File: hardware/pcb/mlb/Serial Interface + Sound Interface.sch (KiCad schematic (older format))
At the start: 52 parts, among them J1 Phone Jack, J11 Speaker, J2 SERIAL_CONN, J3 SERIAL_CONN, Q1 2N3904, Q2 2N3906, Y3 16.9344MHz

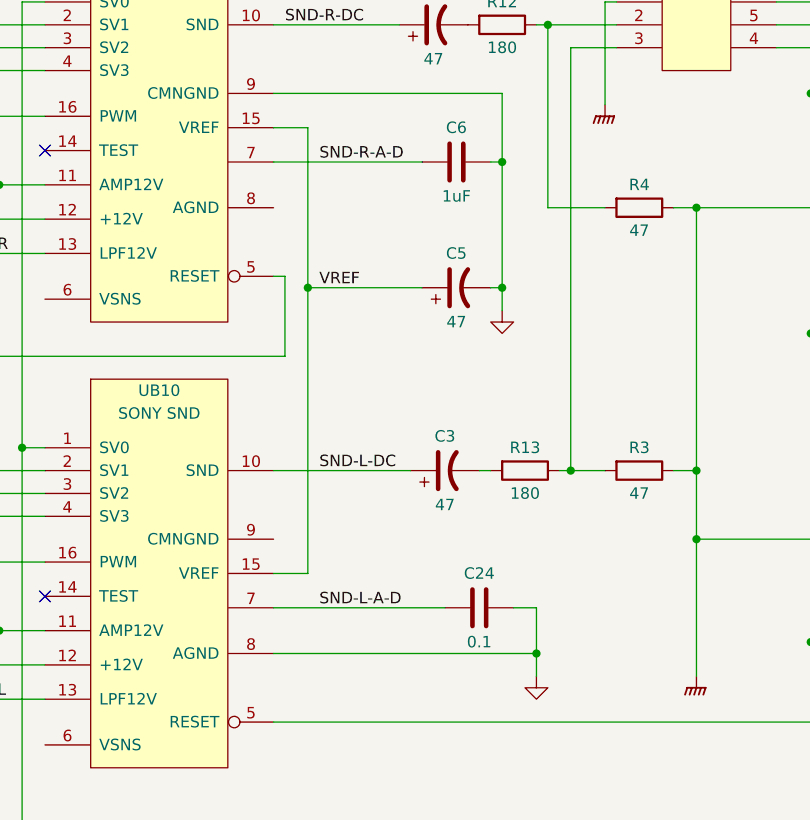
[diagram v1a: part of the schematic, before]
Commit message: Fix missing ground wires, fix some missing reference designators.
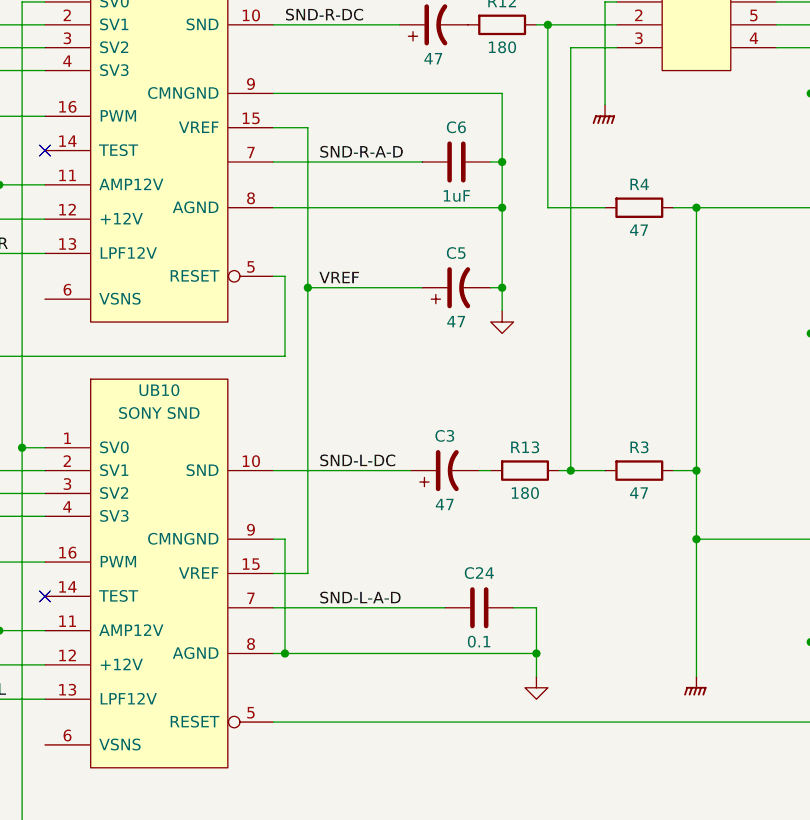
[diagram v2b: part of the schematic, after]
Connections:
- net GND: now also UB10.9 (CMNGND), UB11.8 (AGND)
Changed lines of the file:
@@
 Connection ~ 11850 6750
 Wire Wire Line
-	11850 6750 11850 7300
+	11850 6750 11850 6950
 Wire Wire Line
 	11800 7300 11850 7300
@@
 $EndComp
 Wire Wire Line
-	10850 8900 12000 8900
+	10850 8900 10900 8900
 Wire Wire Line
 	11900 8700 12000 8700
@@
 Wire Bus Line
 	2200 3200 1350 3200
-Wire Bus Line
-	2050 2900 2050 9200
-Wire Bus Line
-	2200 3200 2200 7900
 Text Notes 16195 735  0    50   ~ 0
 (8)
@@
 Text Notes 1010 735  2    50   ~ 0
 (8)
+Wire Wire Line
+	10850 6950 11850 6950
+Connection ~ 11850 6950
+Wire Wire Line
+	11850 6950 11850 7300
+Wire Wire Line
+	10850 8400 10900 8400
+Wire Wire Line
+	10900 8400 10900 8900
+Wire Bus Line
+	2050 2900 2050 9200
+Wire Bus Line
+	2200 3200 2200 7900
+Connection ~ 10900 8900
+Wire Wire Line
+	10900 8900 12000 8900
 $EndSCHEMATC

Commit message: Correct transcription error DSC to OSC.
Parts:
- UE10: value DSC -> OSC; symbol Macintosh_SE_30_Components:DSC -> Macintosh_SE_30_Components:OSC
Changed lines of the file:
@@
 NoConn ~ 3750 7800
 $Comp
-L Macintosh_SE_30_Components:DSC UE10
+L Macintosh_SE_30_Components:OSC UE10
 U 1 1 5EC30FDA
 P 3200 6950
 F 0 "UE10" H 3200 6850 50  0000 C CNN
-F 1 "DSC" H 3200 6750 50  0000 C CNN
+F 1 "OSC" H 3200 6750 50  0000 C CNN
 F 2 "" H 3200 6950 50  0001 C CNN
 F 3 "" H 3200 6950 50  0001 C CNN

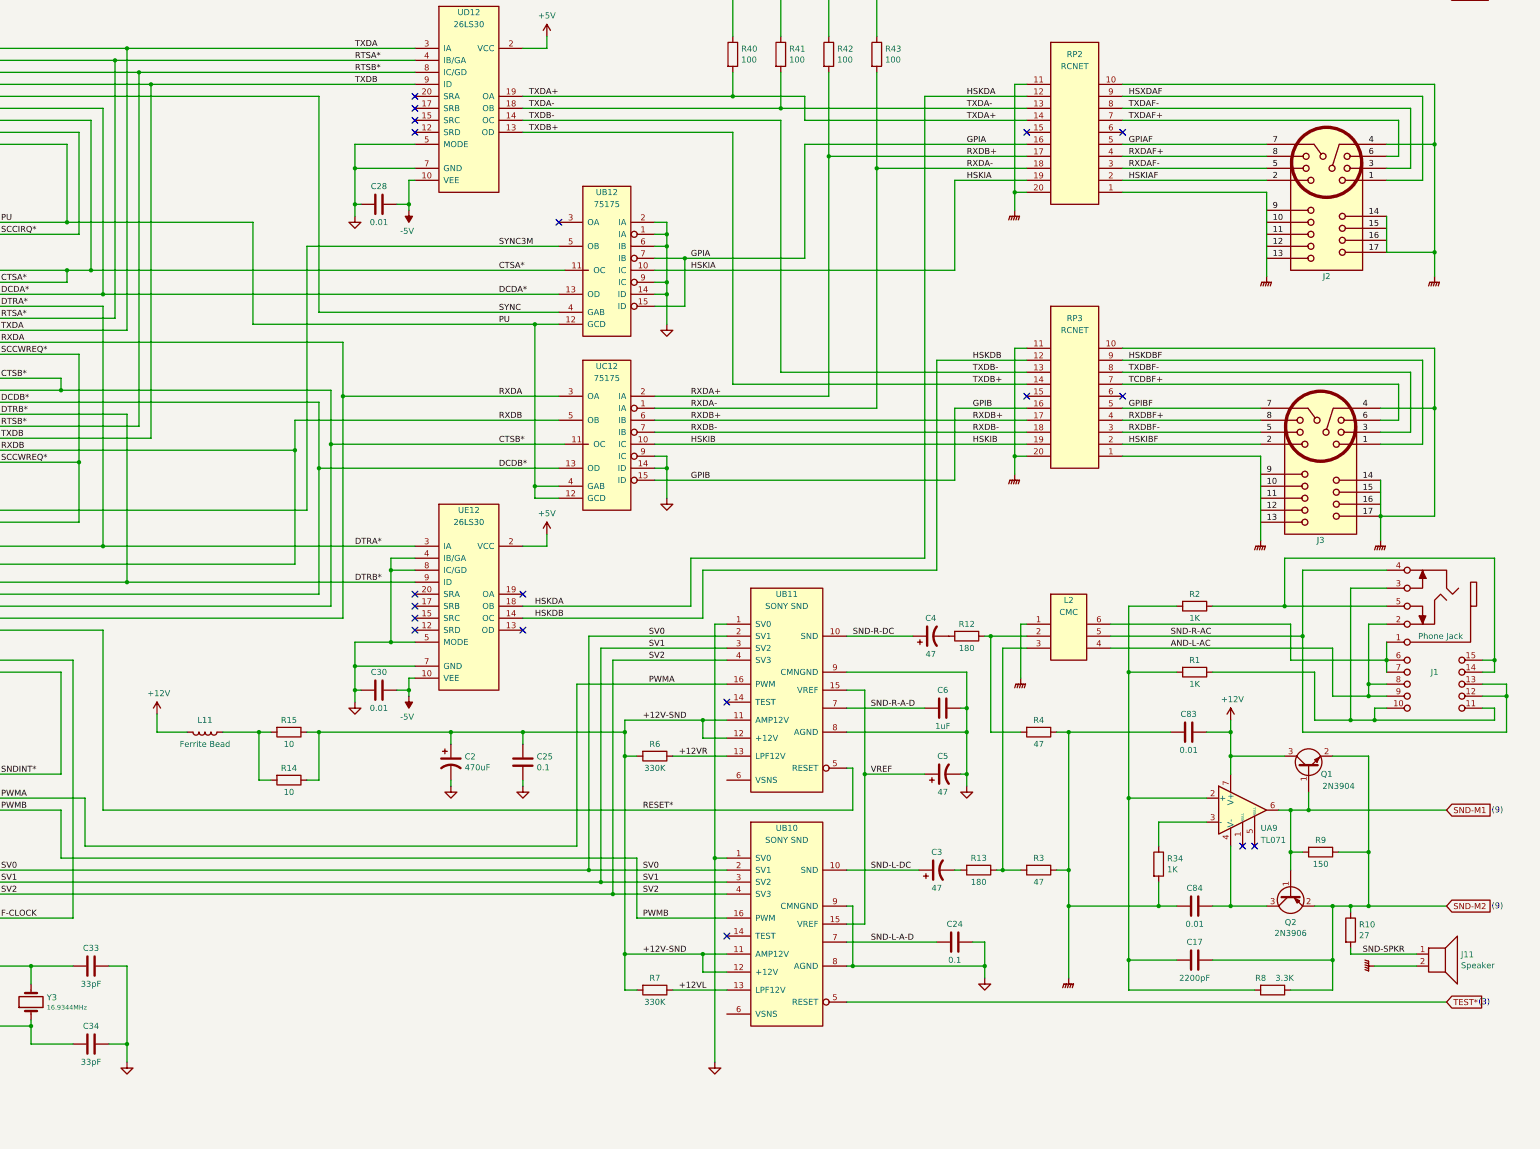
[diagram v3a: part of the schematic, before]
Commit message: Fix errors found in review of the Macintosh SE/30 schematic redraw.
Page 1:

* DSACK*(0:1) (syntax)
* R-W* (inconsistent syntax)
* IPL different syntax
* PDS 38, C16M not grounded
* PDS 39, should be grounded

Page 2:

* RAAF*(8), RABF*(9), RAAF*(10), RABF*(10) (syntax)
* RCMUX* (syntax)
* ROM* missing page 3 indicator
* ROMSIMM1 GND 10, 30, 64
* ROMSIMM1 Incorrect +5V lines
* ROMSIMM1 Confusing bus line drawing angles makes connections look
  duplicated

Page 3:

* VIAIRQ2* (syntax)
* VIAIRQ1N (syntax, on GLUE template)
* SCCRD* (syntax)

Page 4:

* VIA template, RS0, RS1, RS2, RS3 erroneously written as R50, R51,
  R52, R53
* V1PB7 erroneously written as VIPB7
* RTC-D erroneously written as RTC-O
* V1PA0, V1PA1, V1PA2 erroneously written as VIPA0, VIPA1, VIPA2
* warning: additional label BATT not present
* UL11 ADB template, P5 erroneously written as P2
* ADBO erroneously written as ADB0
* SNDINT* erroneously written as SNTINT*

Page 5:

* HSYNC* on UG7 (syntax)
* UJ6 confusing bus line makes signals look duplicated
* Video ROM UK6 not labeled with reference designator (already inside
  KiCad file, stale PDF?)
* VIDS4, VIDS3, VIDS2, VIDS1, VIDS0 erroneously written a VID54,
  VID53, VID53, VID51, VID50
* R-W* alternate page reference erroneously written as RW*
* 74F253 template, G erroneously labeled as GND
* 74F253 template, missing second G enable pin
* style: C0 in 74F253 template should not be C0(GND)
* warning: UA8 ALTVID line could have another label close to the chip

Page 6:

* warning: On SWIM, WRDATA could have label WR*
* DB25 connector: DP*, DB0*, DB1*, DB2*, DB3*, DB4*, DB5*, DB6*, DB7*
  (syntax)
* J8 Ribbon Connector: Missing +12V on 13, 15, 17, 19
* J6 DB-19: Missing +12V-DSK on 7, 8
* warning: missing RDDATA.F additional label near J6 DB-19 pin 18
* warning: missing WRITE.F additional label near J6 DB-19 pin 19
* warning: confusing bus line layout on 53C80 looks like duplicate
  wiring

Page 7:

* RXDA+ erroneously written as RXDB+
* HSKOA erroneo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
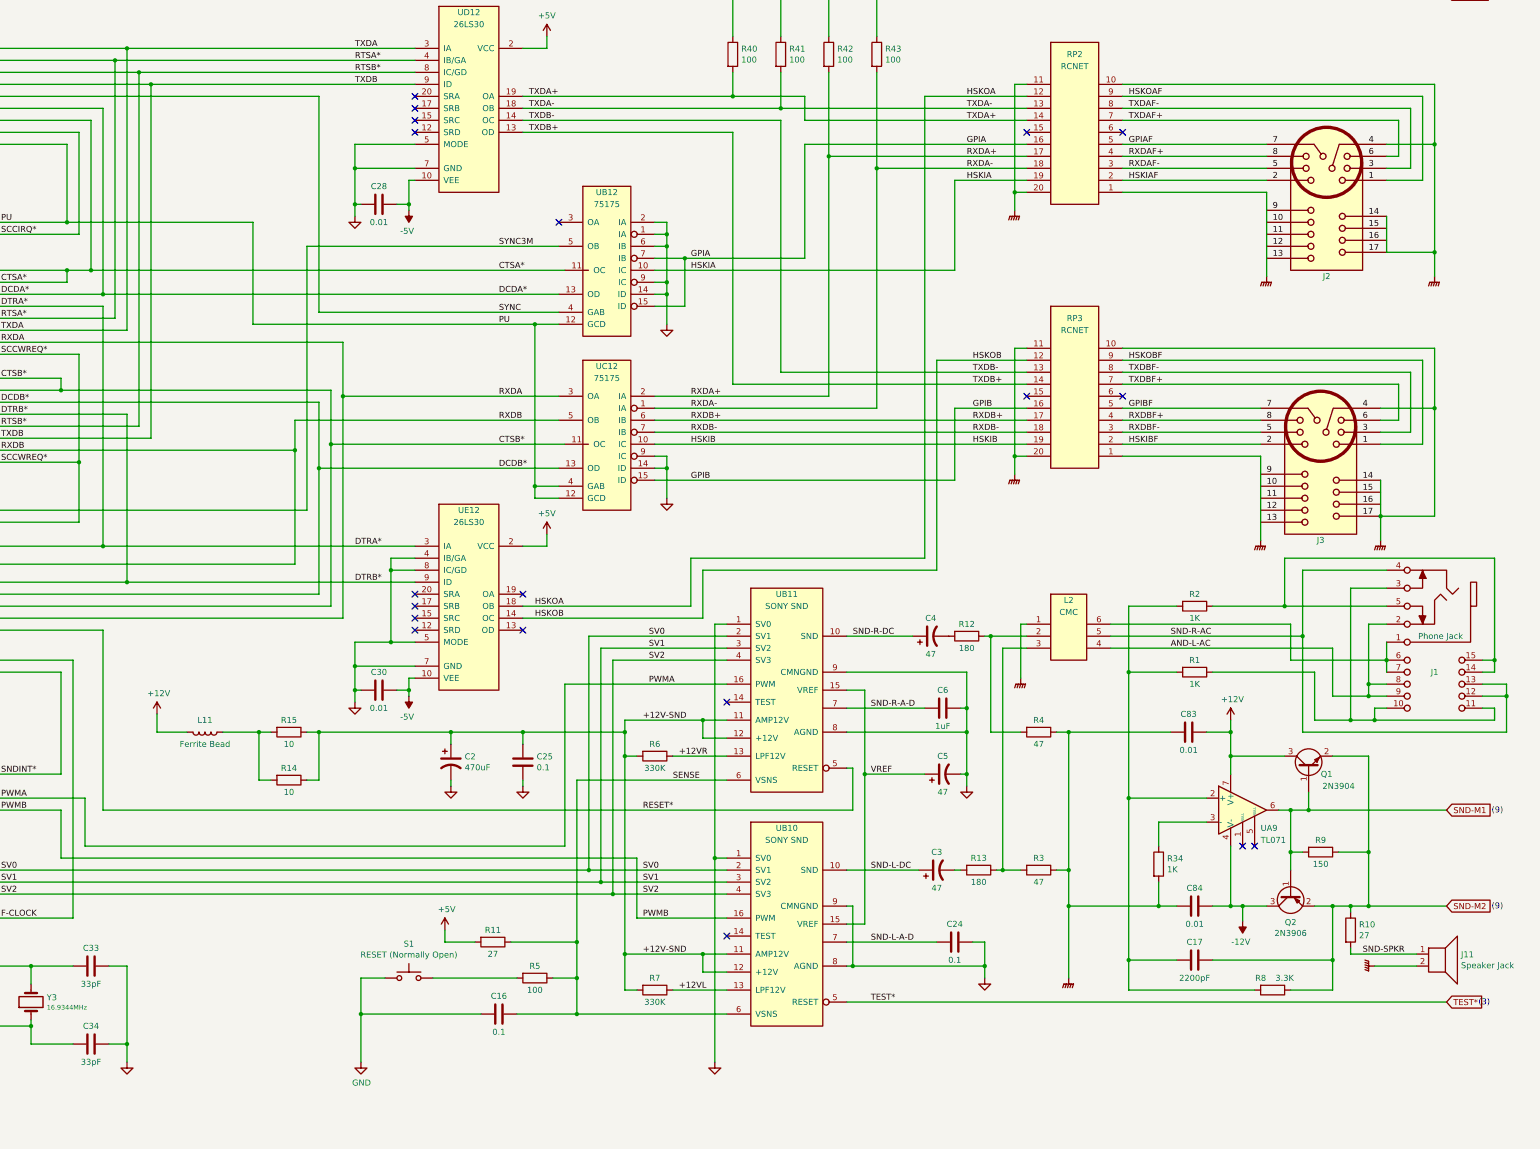
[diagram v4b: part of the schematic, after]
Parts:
- added C16: 0.1, symbol Device:C
- added R11: 27, symbol Device:R
- added R5: 100, symbol Device:R
- added S1: RESET (Normally Open), symbol Switch:SW_MEC_5G
- J11: value Speaker -> Speaker Jack
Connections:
- net +5V: now also R11.2
- net GND: now also C16.2, S1.1 (A), S1.2 (A)
- net RXDA+: no longer RP3.17, UC12.6 (IB)
- net SENSE: now reaches UB11.6 (VSNS)
- net SENSE: now also UB10.6 (VSNS), C16.1, R11.1, R5.1
- net -12V: now reaches C84.1, Q2.3 (E), UA9.4 (V-)
- net HSKDA renamed HSKOA
- net HSKDB renamed HSKOB
- net HSKDBF renamed HSKOBF
- net HSXDAF renamed HSKOAF
- net TCDBF+ renamed TXDBF+
- new net: R5.2, S1.3 (B), S1.4 (B)
- new net RXDB+: RP3.17, UC12.6 (IB)
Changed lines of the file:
@@
 U 1 1 5EC30DA6
 P 3200 2450
+AR Path="/5EC30DA6" Ref="UG12"  Part="1"
+AR Path="/5EC6E3D0/5EC30DA6" Ref="UG12"  Part="1"
 F 0 "UG12" H 3200 2550 50  0000 C CNN
 F 1 "8530" H 3200 2450 50  0000 C CNN
@@
 U 1 1 5EC34042
 P 8850 2550
+AR Path="/5EC34042" Ref="UB12"  Part="1"
+AR Path="/5EC6E3D0/5EC34042" Ref="UB12"  Part="1"
 F 0 "UB12" H 8850 2650 50  0000 C CNN
 F 1 "75175" H 8850 2550 50  0000 C CNN
@@
 U 1 1 5EC340B3
 P 8850 4000
+AR Path="/5EC340B3" Ref="UC12"  Part="1"
+AR Path="/5EC6E3D0/5EC340B3" Ref="UC12"  Part="1"
 F 0 "UC12" H 8850 4100 50  0000 C CNN
 F 1 "75175" H 8850 4000 50  0000 C CNN
@@
 	4500 7500 4500 7900
 Wire Wire Line
-	4500 7900 8600 7900
+	4500 7900 8500 7900
 Wire Wire Line
-	8600 7900 8600 6550
+	8500 7900 8500 6550
 Wire Wire Line
-	8600 6550 9850 6550
+	8500 6550 9850 6550
 Text Label 9200 6550 0    50   ~ 0
 PWMA
@@
 Connection ~ 14050 8400
 Wire Wire Line
-	14050 8400 14350 8400
+	14050 8400 14150 8400
 $Comp
 L Macintosh_SE_30_Components:2N3906 Q2
@@
 	0    1    1    0
 $EndComp
-$Comp
-L Device:Speaker J11
-U 1 1 5F089CF2
-P 15800 8800
-F 0 "J11" H 15970 8796 50  0000 L CNN
-F 1 "Speaker" H 15970 8705 50  0000 L CNN
-F 2 "" H 15800 8600 50  0001 C CNN
-F 3 "~" H 15790 8750 50  0001 C CNN
-	1    15800 8800
-	1    0    0    -1
-$EndComp
 Text Label 15150 8800 0    50   ~ 0
 SND-SPKR
@@
 RXDA-
 Text Label 11850 2150 0    50   ~ 0
-RXDB+
+RXDA+
 Text Label 11850 2050 0    50   ~ 0
 GPIA
@@
 TXDA-
 Text Label 11850 1650 0    50   ~ 0
-HSKDA
+HSKOA
 Text Label 9550 3000 0    50   ~ 0
 GPIA
@@
 	9650 5600 11600 5600
 Text Label 11900 3850 0    50   ~ 0
-HSKDB
+HSKOB
 Text Label 8250 5900 0    50   ~ 0
-HSKDA
+HSKOA
 Text Label 8250 6000 0    50   ~ 0
-HSKDB
+HSKOB
 Wire Wire Line
 	9900 800  1350 800
@@
 $EndComp
 Text Label 13200 1650 0    50   ~ 0
-HSXDAF
+HSKOAF
 Text Label 13200 1750 0    50   ~ 0
 TXDAF-
@@
 	15750 4250 15750 5150
 Text Label 13200 3850 0    50   ~ 0
-HSKDBF
+HSKOBF
 Text Label 13200 3950 0    50   ~ 0
 TXDBF-
 Text Label 13200 4050 0    50   ~ 0
-TCDBF+
+TXDBF+
 Text Label 13200 4250 0    50   ~ 0
 GPIBF
@@
 Wire Wire Line
 	10900 8400 10900 8900
+Connection ~ 10900 8900
+Wire Wire Line
+	10900 8900 12000 8900
+$Comp
+L power:-12V #PWR?
+U 1 1 606E34BB
+P 14150 8525
+F 0 "#PWR?" H 14150 8625 50  0001 C CNN
+F 1 "-12V" H 14165 8698 50  0000 C CNN
+F 2 "" H 14150 8525 50  0001 C CNN
+F 3 "" H 14150 8525 50  0001 C CNN
+	1    14150 8525
+	-1   0    0    1
+$EndComp
+Connection ~ 14150 8400
+Wire Wire Line
+	14150 8400 14350 8400
+Wire Wire Line
+	14150 8525 14150 8400
+$Comp
+L Device:Speaker J11
+U 1 1 5F089CF2
+P 15800 8800
+F 0 "J11" H 15970 8796 50  0000 L CNN
+F 1 "Speaker Jack" H 15970 8705 50  0000 L CNN
+F 2 "" H 15800 8600 50  0001 C CNN
+F 3 "~" H 15790 8750 50  0001 C CNN
+	1    15800 8800
+	1    0    0    -1
+$EndComp
+$Comp
+L Device:R R11
+U 1 1 6086FEE8
+P 7900 8700
+F 0 "R11" V 7800 8700 50  0000 C CNN
+F 1 "27" V 8000 8700 50  0000 C CNN
+F 2 "" V 7830 8700 50  0001 C CNN
+F 3 "~" H 7900 8700 50  0001 C CNN
+	1    7900 8700
+	0    1    1    0
+$EndComp
+$Comp
+L Device:C C16
+U 1 1 608F0E76
+P 7950 9300
+F 0 "C16" V 7800 9300 50  0000 C CNN
+F 1 "0.1" V 8100 9300 50  0000 C CNN
+F 2 "" H 7988 9150 50  0001 C CNN
+F 3 "~" H 7950 9300 50  0001 C CNN
+	1    7950 9300
+	0    1    1    0
+$EndComp
+$Comp
+L power:GND #PWR?
+U 1 1 609342BB
+P 6800 9700
+F 0 "#PWR?" H 6800 9450 50  0001 C CNN
+F 1 "GND" H 6805 9527 50  0000 C CNN
+F 2 "" H 6800 9700 50  0001 C CNN
+F 3 "" H 6800 9700 50  0001 C CNN
+	1    6800 9700
+	1    0    0    -1
+$EndComp
+$Comp
+L Switch:SW_MEC_5G S1
+U 1 1 609B70E2
+P 7200 9000
+F 0 "S1" H 7200 9285 50  0000 C CNN
+F 1 "RESET (Normally Open)" H 7200 9194 50  0000 C CNN
+F 2 "" H 7200 9200 50  0001 C CNN
+F 3 "http://www.apem.com/int/index.php?controller=attachment&id_attachment=488" H 7200 9200 50  0001 C CNN
+	1    7200 9000
+	1    0    0    -1
+$EndComp
+$Comp
+L power:+5V #PWR?
+U 1 1 609B8E47
+P 7500 8600
+F 0 "#PWR?" H 7500 8450 50  0001 C CNN
+F 1 "+5V" H 7515 8773 50  0000 C CNN
+F 2 "" H 7500 8600 50  0001 C CNN
+F 3 "" H 7500 8600 50  0001 C CNN
+	1    7500 8600
+	1    0    0    -1
+$EndComp
+Wire Wire Line
+	7500 8600 7500 8700
+Wire Wire Line
+	7500 8700 7750 8700
+Wire Wire Line
+	8100 9000 7400 9000
+Wire Wire Line
+	7000 9000 6800 9000
+Wire Wire Line
+	6800 9000 6800 9300
+Wire Wire Line
+	7800 9300 6800 9300
+Connection ~ 6800 9300
+Wire Wire Line
+	6800 9300 6800 9700
+Wire Wire Line
+	9850 9300 8600 9300
+Wire Wire Line
+	9850 7350 8600 7350
+Wire Wire Line
+	8600 7350 8600 8700
+Connection ~ 8600 9300
+Wire Wire Line
+	8600 9300 8100 9300
+Wire Wire Line
+	8400 9000 8600 9000
+Connection ~ 8600 9000
+Wire Wire Line
+	8600 9000 8600 9300
+Wire Wire Line
+	8050 8700 8600 8700
+Connection ~ 8600 8700
+Wire Wire Line
+	8600 8700 8600 9000
+$Comp
+L Device:R R5
+U 1 1 608B047C
+P 8250 9000
+F 0 "R5" V 8150 9000 50  0000 C CNN
+F 1 "100" V 8350 9000 50  0000 C CNN
+F 2 "" V 8180 9000 50  0001 C CNN
+F 3 "~" H 8250 9000 50  0001 C CNN
+	1    8250 9000
+	0    1    1    0
+$EndComp
+Text Label 9400 7350 0    50   ~ 0
+SENSE
+Text Label 11050 9200 0    50   ~ 0
+TEST*
 Wire Bus Line
 	2050 2900 2050 9200
 Wire Bus Line
 	2200 3200 2200 7900
-Connection ~ 10900 8900
-Wire Wire Line
-	10900 8900 12000 8900
 $EndSCHEMATC
